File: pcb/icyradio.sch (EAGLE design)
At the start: 360 parts, among them J701 TRSJACK, J702 TRSJACK, J703 TRSJACK, Q801 AO3400, Q802 AO3400, U1001 MIC23155, U1002 MIC23159, U1003 MIC2019, U1004 ADP150UJZ-1.8, U1005 ADP150UJZ-3.3, U1006 MIC94305, U1007 MIC94305, U101 EFM32GG11B420F2048GL112, U201 ATSAMS70Q21B-C, U301 ICE40HX8K-CT256, U401 DSC1211DE3-C0017, U402 LTC2206, U403 RT820T2, U501 ADL5385, U502 AD9117, U503 ADL5601, U601 DSC1201DE3-50M00000, U602 ADF4351, U701 TSCS25A3X1NDGXZAX, U702 CP2615, U801 ER-TFT035-6, U901 DSC1201DE3-50M00000, U902 SI5351C, X101 32.768 kHz, X401 DNP, X901 DNP

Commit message: PCB needs machine gunning
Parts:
- added C528: 200pF, Capacitor:CAPACITOR-0603
- added CON301: FPC-40P, Generic Connector:FPC-40P
- added D1002, D1003, D101, D201, D501, D702: LED0603, LED:LED0603
- added D301: RGBLED, LED:RGBLED
- added R1015: 820 Ohms, Resistor:RESISTOR-0603
- added R1016: 100K Ohms, Resistor:RESISTOR-0603
- added R106, R204: 10K Ohms, Resistor:RESISTOR-0603
- added R302, R303, R304: 330 Ohms, Resistor:RESISTOR-0603
- added R516: 100 Ohms, Resistor:RESISTOR-0603
- added R722: 3.57 Ohms, Resistor:RESISTOR-0603
- added TP1, TP2, TP3: TESTPOINT-0.7MM, PADs:TESTPOINT-0.7MM
- C516: value 200pF -> 100nF
- C520: value 620pF -> 200pF
- C524: value 200pF -> 620pF
- R1012: value 100K Ohms -> 510 Ohms
- R1013: value 820 Ohms -> 330 Ohms
- R103: value 4.7K Ohms -> 330 Ohms
- R105, R711: value 10K Ohms -> 4.7K Ohms
- R203: value 10K Ohms -> 330 Ohms
- R508: value 50 Ohms -> 510 Ohms
- R512: value 10K Ohms -> 50 Ohms
- R514, R707: value 100 Ohms -> 10K Ohms
- R704: value 24K Ohms -> 510 Ohms
- R705: value 47K Ohms -> 24K Ohms
- R706: value 10K Ohms -> 47K Ohms
- R708: value 2.21K Ohms -> 100 Ohms
- R709, R713: value 4.7K Ohms -> 2.21K Ohms
- R712: value 2.21K Ohms -> 10K Ohms
- R715: value 100 Ohms -> 4.7K Ohms
- R716: value 600 Ohms -> 100 Ohms
- R718, R721: value 3.57 Ohms -> 600 Ohms
- R719: value 600 Ohms -> 3.57 Ohms
- renumbered SJ1 to SJ201
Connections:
- net !DSP_SPI_SS renamed !DSP_SPI_CS
- new net DSP_LED: R203.2, U201.PIOB.PB4
- new net FPGA_BLED: R304.1, U301.BANK1.IOR_165
- new net FPGA_GLED: R303.1, U301.BANK0.IOT_177
- new net FPGA_RLED: R302.1, U301.BANK0.IOT_176
- new net N$105: CON301-5.S, U301.BANK3.IOL_6B
- new net N$106: CON301-4.S, U301.BANK3.IOL_1A
- new net N$107: CON301-3.S, U301.BANK0.IOT_225
- new net N$108: CON301-6.S, U301.BANK3.IOL_7B
- new net N$109: CON301-9.S, U301.BANK3.IOL_10B
- new net N$110: CON301-8.S, U301.BANK3.IOL_9B
- new net N$111: CON301-7.S, U301.BANK3.IOL_8B
- new net N$112: CON301-10.S, U301.BANK3.IOL_11B
- new net N$113: CON301-12.S, U301.BANK3.IOL_12B
- new net N$114: CON301-11.S, U301.BANK3.IOL_13B_GBIN7
- new net N$115: CON301-13.S, U301.BANK3.IOL_14B
- new net N$116: CON301-16.S, U301.BANK3.IOL_15A
- new net N$117: CON301-15.S, U301.BANK3.IOL_15B
- new net N$118: CON301-14.S, U301.BANK3.IOL_9A
- new net N$119: CON301-18.S, U301.BANK3.IOL_17B
- new net N$120: CON301-17.S, U301.BANK3.IOL_16A
- new net N$121: CON301-23.S, U301.BANK3.IOL_16B
- new net N$122: CON301-26.S, U301.BANK3.IOL_19B
- new net N$123: CON301-24.S, U301.BANK3.IOL_18A
- new net N$124: CON301-25.S, U301.BANK3.IOL_17A
- new net N$125: CON301-27.S, U301.BANK3.IOL_18B
- new net N$126: CON301-28.S, U301.BANK3.IOL_20B
- new net N$127: CON301-29.S, U301.BANK3.IOL_22B
- new net N$128: CON301-30.S, U301.BANK3.IOL_24B
- new net N$129: CON301-31.S, U301.BANK3.IOL_25B
- new net N$130: CON301-33.S, U301.BANK3.IOL_22A
- new net N$131: CON301-32.S, U301.BANK3.IOL_23A
- new net N$132: CON301-37.S, U301.BANK3.IOL_19A
- new net N$133: CON301-34.S, U301.BANK2SPI.IOB_54
- new net N$134: CON301-35.S, U301.BANK2SPI.IOB_58
- new net N$135: CON301-36.S, U301.BANK2SPI.IOB_52
- new net N$136: CON301-38.S, U301.BANK2SPI.IOB_66
- new net N$137: C516.C1, U502.REFIO
- new net N$138: TP1.TP, U201.PWRCTRL.JTAGSEL
- new net N$139: TP2.TP, U201.PWRCTRL.TST
- new net N$140: TP3.TP, U301.PWRCTRL.VPP_FAST
- new net N$141: D301R.A, R302.2
- new net N$142: D301G.A, R303.2
- new net N$143: D301B.A, R304.2
- new net N$144: D101.A, R103.1
- new net N$145: D201.A, R203.1
- new net N$146: D501.A, R508.1
- new net N$147: D702.A, R704.1
- new net N$148: D1003.A, R1013.1
- new net N$149: D1002.A, R1012.1
- new net SMC_LED: R103.2, U101.PA15
- net !DSP_RESET: now also R204.1, U101.PB10; no longer R203.1
- net !I2S_BRG_CFG: now also R707.1; no longer R706.1
- net !I2S_BRG_RST: now also R712.1; no longer R711.1
- net !SMC_RESET: now also R106.1; no longer R105.1
- net !TXPA_OC: now also R1016.1; no longer R1014.1
- net 3V3: now also CON301-1.S, CON301-20.S, CON301-21.S, CON301-40.S, R1013.2, R1016.2, R106.2, R204.2, R707.2, R712.2; no longer R1014.2, R103.2, R203.2, R706.2, R711.2
- net 5V0: now also R1012.2
- net 5V0_ANA_TXPA_CLEAN: now also R508.2
- net AUDIO_I2C_SCL: now also R105.1; no longer R104.1
- net AUDIO_I2C_SDA: now also R104.1; no longer R103.1
- net CODEC_HP_L: now also R722.1; no longer R721.1
- net CODEC_HP_R: now also R719.1; no longer R718.1
- net CODEC_LINE_L: now also R721.1; no longer R720.1
- net CODEC_LINE_R: now also R718.1; no longer R717.1
- net CODEC_MIC_L: now also R720.1; no longer R719.1
- net CODEC_MIC_R: now also R717.1; no longer R716.1
- net GND: now also C517.C2, C518.C1, C519.C2, C520.C1, C521.C2, C522.C1, C523.C2, C524.C1, C525.C2, C526.C1, C527.C2, C528.C1, CON301-19.S, CON301-2.S, CON301-22.S, CON301-39.S, D1002.C, D1003.C, D101.C, D201.C, D301B.C, D301G.C, D301R.C, D501.C, D702.C, R1014.1, R1015.1, R509.1, R510.2, R511.1, R512.2, R706.1, R708.1, R711.1, R716.1; no longer C517.C1, C518.C2, C519.C1, C520.C2, C521.C1, C522.C2, C523.C1, C524.C2, C525.C1, C526.C2, C527.C1, R1012.1, R1013.1, R508.1, R509.2, R510.1, R511.2, R705.1, R707.1, R709.1, R713.1
- net I2S_BRG_VBUS: now also R705.2
- net I2S_BRG_VBUS_DET: now also R705.1, R706.2; no longer R704.1, R705.2
- net N$38: now also R709.1, R710.2, R717.2; no longer R708.1, R709.2, R716.2
- net N$39: now also R713.1, R714.2, R720.2; no longer R712.1, R713.2, R719.2
- net N$42: now also R711.2, R718.2; no longer R710.2, R717.2
- net N$44: now also R715.2, R721.2; no longer R714.2, R720.2
- net N$50: now also R722.2; no longer R721.2
- net N$52: now also R708.2; no longer R707.2
- net N$53: now also R716.2; no longer R715.2
- net N$54: now also R719.2; no longer R718.2
- net N$55: now also R709.2, R713.2; no longer R708.2, R712.2
- net N$73: now also C518.C2, R510.1; no longer C517.C2, R509.1
- net N$74: now also C517.C1, R509.2; no longer C516.C1, R508.2
- net N$75: now also C522.C2; no longer C521.C2
- net N$76: now also C521.C1; no longer C520.C1
- net N$80: now also C520.C2, R512.1; no longer C519.C2, R511.1
- net N$81: now also C519.C1, R511.2; no longer C518.C1, R510.2
- net N$82: now also C524.C2; no longer C523.C2
- net N$83: now also C523.C1; no longer C522.C1
- net N$94: now also R1015.2; no longer R1013.2
- net TXDAC_AUXI: now also R513.2; no longer R512.2
- net TXDAC_AUXQ: now also R514.2; no longer R513.2
- net TXMIXER_IBBN: now also C525.C1, R515.2; no longer C524.C1, R514.2
- net TXMIXER_IBBP: now also C526.C2, R513.1, R515.1; no longer C525.C2, R512.1, R514.1
- net TXMIXER_QBBN: now also C527.C1, R516.2; no longer C526.C1, R515.2
- net TXMIXER_QBBP: now also C528.C2, R514.1, R516.1; no longer C527.C2, R513.1, R515.1
- net TXPA_BIAS_EN: now also R1014.2; no longer R1012.2
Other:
- moved on the sheet: C516, C517, C518, C519, C520, C521, C522, C523, C524, C525, C526, C527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

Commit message: I think it dun
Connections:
- net N$1 renamed SMC_VCORE
- net N$100 renamed TXPLL_REF_DCC
- net N$105 renamed EXP_IO2
- net N$106 renamed EXP_IO1
- net N$107 renamed EXP_IO0
- net N$108 renamed EXP_IO3
- net N$109 renamed EXP_IO6
- net N$11 renamed CLK_MNGR_CLK1
- net N$110 renamed EXP_IO5
- net N$111 renamed EXP_IO4
- net N$112 renamed EXP_IO7
- net N$113 renamed EXP_IO9
- net N$114 renamed EXP_IO8
- net N$115 renamed EXP_IO10
- net N$116 renamed EXP_IO13
- net N$117 renamed EXP_IO12
- net N$118 renamed EXP_IO11
- net N$119 renamed EXP_IO15
- net N$12 renamed CLK_MNGR_CLK2
- net N$120 renamed EXP_IO14
- net N$121 renamed EXP_IO16
- net N$122 renamed EXP_IO19
- net N$123 renamed EXP_IO17
- net N$124 renamed EXP_IO18
- net N$125 renamed EXP_IO20
- net N$126 renamed EXP_IO21
- net N$127 renamed EXP_IO22
- net N$128 renamed EXP_IO23
- net N$129 renamed EXP_IO24
- net N$13 renamed CLK_MNGR_CLK3
- net N$130 renamed EXP_IO26
- net N$131 renamed EXP_IO25
- net N$132 renamed EXP_IO30
- net N$133 renamed EXP_IO27
- net N$134 renamed EXP_IO28
- net N$135 renamed EXP_IO29
- net N$136 renamed EXP_IO31
- net N$138 renamed DSP_JTAGSEL
- net N$139 renamed DSP_TST
- net N$14 renamed CLK_MNGR_CLK5
- net N$140 renamed FPGA_VPP_FAST
- net N$19 renamed CLK_MNGR_CLK6
- net N$2 renamed TXMIXER_OUT
- net N$24 renamed TFT_BL_K2
- net N$25 renamed TFT_BL_K1
- net N$28 renamed RXADC_SENSE
- net N$31 renamed CODEC_CAP-
- net N$32 renamed CPDEC_CAP+
- net N$33 renamed CODEC_V-
- net N$34 renamed CODEC_VREF
- net N$35 renamed CODEC_AFILT2
- net N$36 renamed CODEC_AFILT1
- net N$40 renamed 3V3_SOFTSTART
- net N$41 renamed 1V2_SOFTSTART
- net N$57 renamed TXPA_IN
- net N$59 renamed RXADC_ENC+
- net N$60 renamed CLK_MNGR_REF
- net N$61 renamed CLK_MNGR_XTALB
- net N$62 renamed CLK_MNGR_XTALA
- net N$66 renamed 3V6_ANA_SOFTSTART
- net N$7 renamed CLK_MNGR_CLK0
- net N$78 renamed TXPLL_CP_VOUT
- net N$79 renamed TXPLL_VTUNE
- net N$85 renamed TXPLL_TEMP
- net N$86 renamed TXPLL_VCOM
- net N$87 renamed TXPLL_VREF
- net N$89 renamed TXPLL_REF_ACC
- net N$90 renamed TXPA_OUT
- net N$91 renamed DSP_VDDPLLUSB
- net N$99 renamed TXPLL_FASTLOCK_SW
- net RXTUNER_PLL_VDD renamed RXTUNER_VDD_PLL
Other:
- moved on the sheet: C901, C902, C903, C904, C905, C906, C907, R901, R902, R903, R904, R905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

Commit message: Added FPGA SPI memory
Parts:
- added C319: 100nF, Capacitor:CAPACITOR-0603
- added R305: 100K Ohms, Resistor:RESISTOR-0603
- added U302: SST26VF064B, Microchip:SST26VF064B
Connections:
- net FPGA_DDC_CLK renamed FPGA_CLK1
- net FPGA_GP_CLK1 renamed FPGA_CLK2
- net FPGA_GP_CLK2 renamed FPGA_CLK3
- net FPGA_GP_CLK3 renamed FPGA_CLK4
- new net !FPGA_DSP_IRQ: U201.PIOC.PC30, U301.BANK1.IOR_147
- new net !FPGA_MEM_CS: R305.1, U301.BANK1.IOR_160, U302.!CS!
- new net FPGA_MEM_IO0: U301.BANK0.IOT_174, U302.MOSI/IO0
- new net FPGA_MEM_IO1: U301.BANK1.IOR_166, U302.MISO/IO1
- new net FPGA_MEM_IO2: U301.BANK1.IOR_167, U302.!WP!/IO2
- new net FPGA_MEM_IO3: U301.BANK0.IOT_170, U302.!HOLD!/IO3
- new net FPGA_MEM_SCK: U301.BANK0.IOT_168, U302.SCK
- net 3V3: now also C319.C1, R305.2, U302.VCC
- net GND: now also C319.C2, U302.GND
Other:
- moved on the sheet: CON301-10, CON301-11, CON301-12, CON301-13, CON301-14, CON301-15, CON301-16, CON301-17, CON301-18, CON301-23, CON301-24, CON301-25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

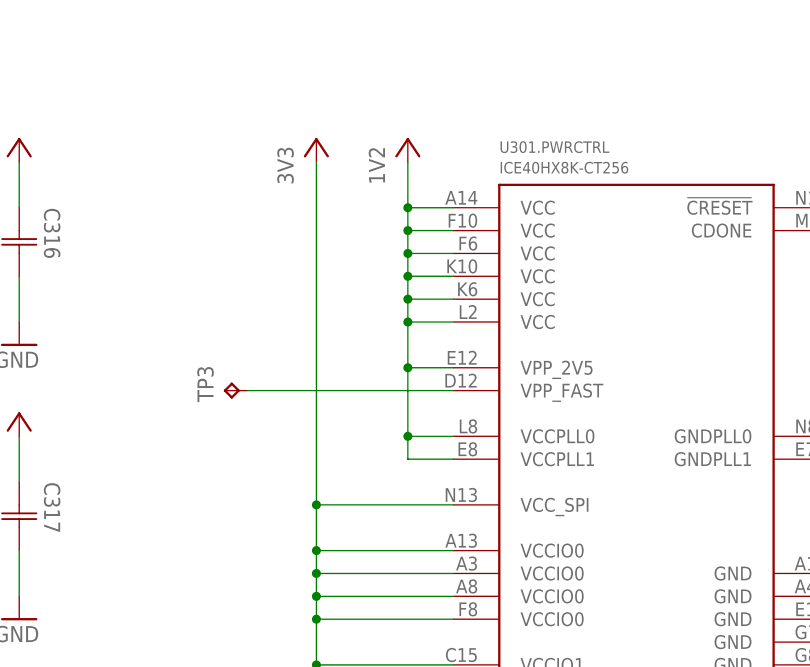
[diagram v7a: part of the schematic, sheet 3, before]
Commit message: Fixed FPGA VCC_2V5 connected to 1V2
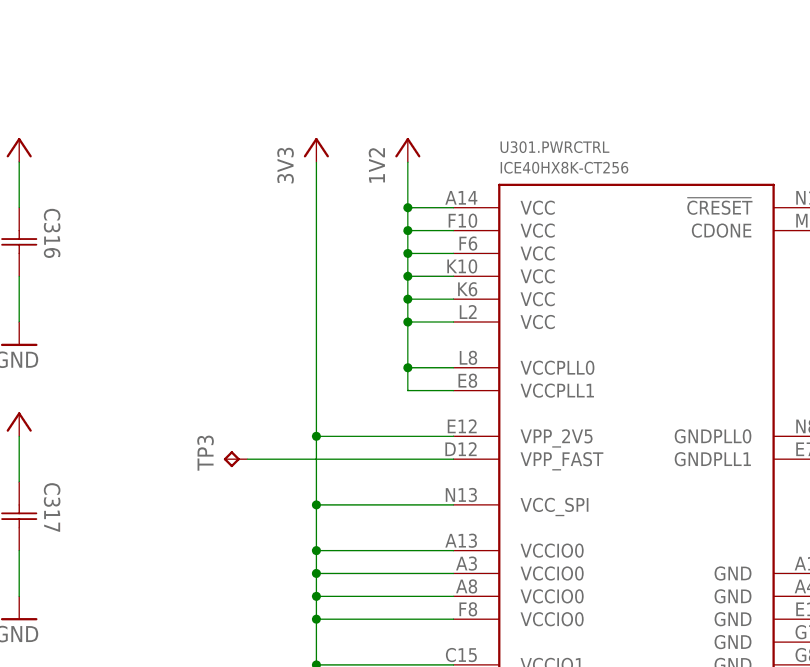
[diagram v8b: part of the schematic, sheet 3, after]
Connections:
- net 1V2: no longer U301.PWRCTRL.VPP_2V5
- net 3V3: now also U301.PWRCTRL.VPP_2V5
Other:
- moved on the sheet: TP3
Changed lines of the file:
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@@
 <attribute name="VALUE" x="508" y="363.22" size="1.778" layer="96" rot="R90"/>
 </instance>
-<instance part="TP3" gate="G$1" x="116.84" y="332.74" smashed="yes" rot="R90">
-<attribute name="NAME" x="115.57" y="331.47" size="1.778" layer="95" rot="R90"/>
+<instance part="TP3" gate="G$1" x="116.84" y="325.12" smashed="yes" rot="R90">
+<attribute name="NAME" x="115.57" y="323.85" size="1.778" layer="95" rot="R90"/>
 </instance>
 <instance part="D301" gate="R" x="375.92" y="332.74" smashed="yes">
@@
 <net name="1V2" class="0">
 <segment>
-<pinref part="U301" gate=".PWRCTRL" pin="VPP_2V5"/>
 <pinref part="1V8309" gate="G$1" pin="1V2"/>
-<wire x1="142.24" y1="335.28" x2="137.16" y2="335.28" width="0.1524" layer="91"/>
-<wire x1="137.16" y1="335.28" x2="137.16" y2="340.36" width="0.1524" layer="91"/>
 <pinref part="U301" gate=".PWRCTRL" pin="VCC@0"/>
 <wire x1="137.16" y1="340.36" x2="137.16" y2="342.9" width="0.1524" layer="91"/>
@@
 <junction x="137.16" y="340.36"/>
 <pinref part="U301" gate=".PWRCTRL" pin="VCCPLL1"/>
-<wire x1="142.24" y1="325.12" x2="137.16" y2="325.12" width="0.1524" layer="91"/>
-<wire x1="137.16" y1="325.12" x2="137.16" y2="327.66" width="0.1524" layer="91"/>
+<wire x1="142.24" y1="332.74" x2="137.16" y2="332.74" width="0.1524" layer="91"/>
+<wire x1="137.16" y1="332.74" x2="137.16" y2="335.28" width="0.1524" layer="91"/>
+<pinref part="U301" gate=".PWRCTRL" pin="VCCPLL0"/>
+<wire x1="137.16" y1="335.28" x2="137.16" y2="340.36" width="0.1524" layer="91"/>
+<wire x1="142.24" y1="335.28" x2="137.16" y2="335.28" width="0.1524" layer="91"/>
 <junction x="137.16" y="335.28"/>
-<pinref part="U301" gate=".PWRCTRL" pin="VCCPLL0"/>
-<wire x1="137.16" y1="327.66" x2="137.16" y2="335.28" width="0.1524" layer="91"/>
-<wire x1="142.24" y1="327.66" x2="137.16" y2="327.66" width="0.1524" layer="91"/>
-<junction x="137.16" y="327.66"/>
 </segment>
 <segment>
@@
 <pinref part="3V3311" gate="G$1" pin="3V3"/>
 <wire x1="142.24" y1="320.04" x2="127" y2="320.04" width="0.1524" layer="91"/>
-<wire x1="127" y1="320.04" x2="127" y2="358.14" width="0.1524" layer="91"/>
+<wire x1="127" y1="320.04" x2="127" y2="327.66" width="0.1524" layer="91"/>
 <pinref part="U301" gate=".PWRCTRL" pin="VCCIO0@0"/>
+<wire x1="127" y1="327.66" x2="127" y2="358.14" width="0.1524" layer="91"/>
 <wire x1="142.24" y1="314.96" x2="127" y2="314.96" width="0.1524" layer="91"/>
 <wire x1="127" y1="314.96" x2="127" y2="320.04" width="0.1524" layer="91"/>
@@
 <wire x1="127" y1="269.24" x2="127" y2="271.78" width="0.1524" layer="91"/>
 <junction x="127" y="271.78"/>
+<pinref part="U301" gate=".PWRCTRL" pin="VPP_2V5"/>
+<wire x1="142.24" y1="327.66" x2="127" y2="327.66" width="0.1524" layer="91"/>
+<junction x="127" y="327.66"/>
 </segment>
 <segment>
@@
 <pinref part="U301" gate=".PWRCTRL" pin="VPP_FAST"/>
 <pinref part="TP3" gate="G$1" pin="TP"/>
-<wire x1="142.24" y1="332.74" x2="119.38" y2="332.74" width="0.1524" layer="91"/>
-</segment>
-</net>
+<wire x1="142.24" y1="325.12" x2="119.38" y2="325.12" width="0.1524" layer="91"/>
+</segment>
+</net>
